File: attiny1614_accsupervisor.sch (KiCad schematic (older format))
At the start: 34 parts, among them J1 VXO7803-500-M-TR, J2 MSTBA_2,5_3-G, J3 Conn_01x02, J4 Conn_02x20_Odd_Even, J5 AVR-UPDI-6, K1 JSM1-12V-5, Q1 BC817, Q2 BC817, Q3 BC817, Q4 BSS84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

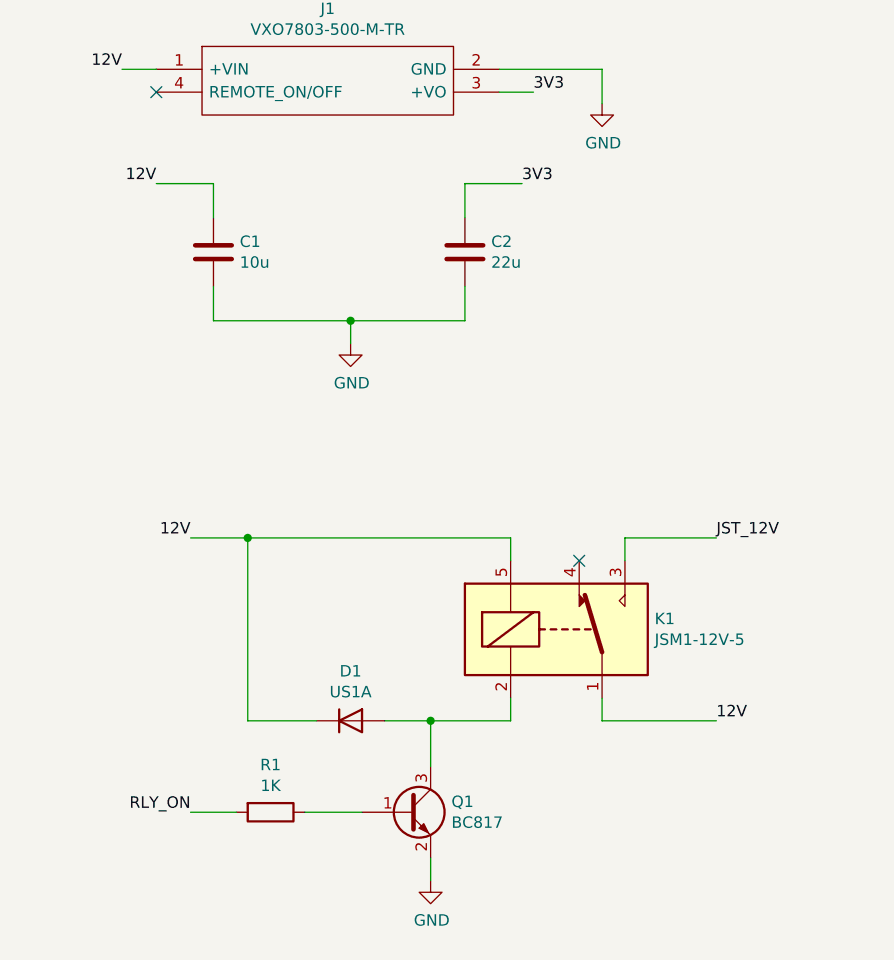
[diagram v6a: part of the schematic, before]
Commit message: BOM consolidation, 10/22uF to 4.7uFs
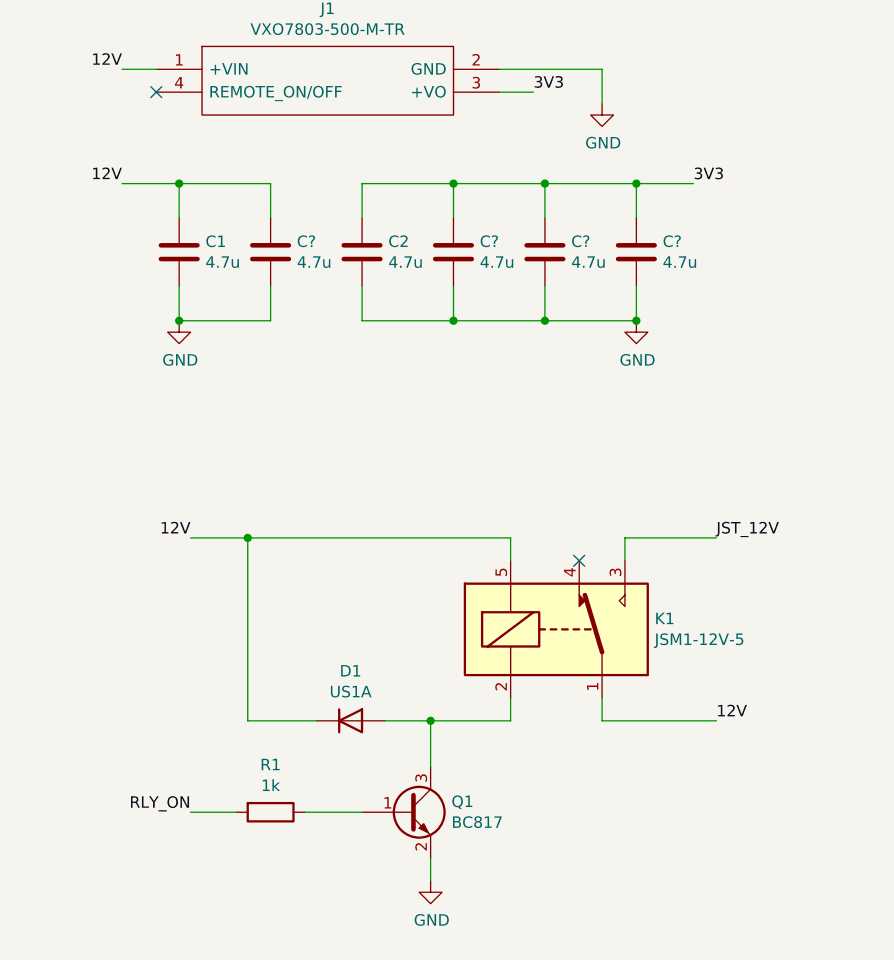
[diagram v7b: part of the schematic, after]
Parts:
- added C? (x4): 4.7u, Capacitor_SMD:C_0805_2012Metric_Pad1.15x1.40mm_HandSolder, symbol Device:C
- C1: value 10u -> 4.7u; footprint Capacitor_SMD:C_1206_3216Metric_Pad1.42x1.75mm_HandSolder -> Capacitor_SMD:C_0805_2012Metric_Pad1.15x1.40mm_HandSolder
- C2: value 22u -> 4.7u; footprint Capacitor_SMD:C_1206_3216Metric_Pad1.42x1.75mm_HandSolder -> Capacitor_SMD:C_0805_2012Metric_Pad1.15x1.40mm_HandSolder
- R1: value 1K -> 1k
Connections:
- net 12V: now also C?.1
- net 3V3: now also C?.1, C?.1, C?.1
- net GND: now also C?.2, C?.2, C?.2, C?.2
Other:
- moved on the sheet: C1, C2
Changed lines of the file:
@@
 P 1750 6150
 F 0 "R1" V 1543 6150 50  0000 C CNN
-F 1 "1K" V 1634 6150 50  0000 C CNN
+F 1 "1k" V 1634 6150 50  0000 C CNN
 F 2 "Resistor_SMD:R_1206_3216Metric_Pad1.42x1.75mm_HandSolder" V 1680 6150 50  0001 C CNN
 F 3 "~" H 1750 6150 50  0001 C CNN
@@
 L Device:C C1
 U 1 1 5F4FA9CB
-P 1500 3700
-F 0 "C1" H 1615 3746 50  0000 L CNN
-F 1 "10u" H 1615 3655 50  0000 L CNN
-F 2 "Capacitor_SMD:C_1206_3216Metric_Pad1.42x1.75mm_HandSolder" H 1538 3550 50  0001 C CNN
-F 3 "~" H 1500 3700 50  0001 C CNN
-	1    1500 3700
+P 1350 3700
+F 0 "C1" H 1465 3746 50  0000 L CNN
+F 1 "4.7u" H 1465 3655 50  0000 L CNN
+F 2 "Capacitor_SMD:C_0805_2012Metric_Pad1.15x1.40mm_HandSolder" H 1388 3550 50  0001 C CNN
+F 3 "~" H 1350 3700 50  0001 C CNN
+	1    1350 3700
 	1    0    0    -1
 $EndComp
@@
 L Device:C C2
 U 1 1 5F4FB924
-P 2600 3700
-F 0 "C2" H 2715 3746 50  0000 L CNN
-F 1 "22u" H 2715 3655 50  0000 L CNN
-F 2 "Capacitor_SMD:C_1206_3216Metric_Pad1.42x1.75mm_HandSolder" H 2638 3550 50  0001 C CNN
-F 3 "~" H 2600 3700 50  0001 C CNN
-	1    2600 3700
-	1    0    0    -1
-$EndComp
-Wire Wire Line
-	1500 3550 1500 3400
-Wire Wire Line
-	1500 3400 1250 3400
-Wire Wire Line
-	1500 3850 1500 4000
-Wire Wire Line
-	1500 4000 2100 4000
-Wire Wire Line
-	2600 4000 2600 3850
-Wire Wire Line
-	2600 3550 2600 3400
-Text Label 1250 3400 2    50   ~ 0
+P 2150 3700
+F 0 "C2" H 2265 3746 50  0000 L CNN
+F 1 "4.7u" H 2265 3655 50  0000 L CNN
+F 2 "Capacitor_SMD:C_0805_2012Metric_Pad1.15x1.40mm_HandSolder" H 2188 3550 50  0001 C CNN
+F 3 "~" H 2150 3700 50  0001 C CNN
+	1    2150 3700
+	1    0    0    -1
+$EndComp
+Wire Wire Line
+	1350 3550 1350 3400
+Wire Wire Line
+	1350 3400 1100 3400
+Wire Wire Line
+	1350 3850 1350 4000
+Wire Wire Line
+	1350 4000 1750 4000
+Wire Wire Line
+	2150 4000 2150 3850
+Wire Wire Line
+	2150 3550 2150 3400
+Text Label 1100 3400 2    50   ~ 0
 12V
-Wire Wire Line
-	2600 3400 2850 3400
-Text Label 2850 3400 0    50   ~ 0
+Text Label 3600 3400 0    50   ~ 0
 3V3
-Wire Wire Line
-	2100 4000 2100 4100
-Connection ~ 2100 4000
-Wire Wire Line
-	2100 4000 2600 4000
 $Comp
 L power:GND #PWR03
 U 1 1 5F5031AF
-P 2100 4100
-F 0 "#PWR03" H 2100 3850 50  0001 C CNN
-F 1 "GND" H 2105 3927 50  0000 C CNN
-F 2 "" H 2100 4100 50  0001 C CNN
-F 3 "" H 2100 4100 50  0001 C CNN
-	1    2100 4100
+P 1350 4000
+F 0 "#PWR03" H 1350 3750 50  0001 C CNN
+F 1 "GND" H 1355 3827 50  0000 C CNN
+F 2 "" H 1350 4000 50  0001 C CNN
+F 3 "" H 1350 4000 50  0001 C CNN
+	1    1350 4000
 	1    0    0    -1
 $EndComp
@@
 NoConn ~ 6250 1750
 NoConn ~ 6250 1850
+$Comp
+L Device:C C?
+U 1 1 5F5B52F6
+P 1750 3700
+F 0 "C?" H 1865 3746 50  0000 L CNN
+F 1 "4.7u" H 1865 3655 50  0000 L CNN
+F 2 "Capacitor_SMD:C_0805_2012Metric_Pad1.15x1.40mm_HandSolder" H 1788 3550 50  0001 C CNN
+F 3 "~" H 1750 3700 50  0001 C CNN
+	1    1750 3700
+	1    0    0    -1
+$EndComp
+Wire Wire Line
+	1750 3850 1750 4000
+Wire Wire Line
+	1750 3550 1750 3400
+Wire Wire Line
+	1750 3400 1350 3400
+Connection ~ 1350 3400
+$Comp
+L power:GND #PWR?
+U 1 1 5F5C8092
+P 3350 4000
+F 0 "#PWR?" H 3350 3750 50  0001 C CNN
+F 1 "GND" H 3355 3827 50  0000 C CNN
+F 2 "" H 3350 4000 50  0001 C CNN
+F 3 "" H 3350 4000 50  0001 C CNN
+	1    3350 4000
+	1    0    0    -1
+$EndComp
+$Comp
+L Device:C C?
+U 1 1 5F5D96DE
+P 2550 3700
+F 0 "C?" H 2665 3746 50  0000 L CNN
+F 1 "4.7u" H 2665 3655 50  0000 L CNN
+F 2 "Capacitor_SMD:C_0805_2012Metric_Pad1.15x1.40mm_HandSolder" H 2588 3550 50  0001 C CNN
+F 3 "~" H 2550 3700 50  0001 C CNN
+	1    2550 3700
+	1    0    0    -1
+$EndComp
+$Comp
+L Device:C C?
+U 1 1 5F5D99D3
+P 2950 3700
+F 0 "C?" H 3065 3746 50  0000 L CNN
+F 1 "4.7u" H 3065 3655 50  0000 L CNN
+F 2 "Capacitor_SMD:C_0805_2012Metric_Pad1.15x1.40mm_HandSolder" H 2988 3550 50  0001 C CNN
+F 3 "~" H 2950 3700 50  0001 C CNN
+	1    2950 3700
+	1    0    0    -1
+$EndComp
+$Comp
+L Device:C C?
+U 1 1 5F5D9D40
+P 3350 3700
+F 0 "C?" H 3465 3746 50  0000 L CNN
+F 1 "4.7u" H 3465 3655 50  0000 L CNN
+F 2 "Capacitor_SMD:C_0805_2012Metric_Pad1.15x1.40mm_HandSolder" H 3388 3550 50  0001 C CNN
+F 3 "~" H 3350 3700 50  0001 C CNN
+	1    3350 3700
+	1    0    0    -1
+$EndComp
+Wire Wire Line
+	2150 3400 2550 3400
+Wire Wire Line
+	2550 3550 2550 3400
+Connection ~ 2550 3400
+Wire Wire Line
+	2550 3400 2950 3400
+Wire Wire Line
+	2950 3550 2950 3400
+Connection ~ 2950 3400
+Wire Wire Line
+	2950 3400 3350 3400
+Wire Wire Line
+	3350 3550 3350 3400
+Connection ~ 3350 3400
+Wire Wire Line
+	3350 3400 3600 3400
+Wire Wire Line
+	3350 3850 3350 4000
+Wire Wire Line
+	3350 4000 2950 4000
+Wire Wire Line
+	2550 3850 2550 4000
+Connection ~ 2550 4000
+Wire Wire Line
+	2550 4000 2150 4000
+Wire Wire Line
+	2950 3850 2950 4000
+Connection ~ 2950 4000
+Wire Wire Line
+	2950 4000 2550 4000
+Connection ~ 1350 4000
+Connection ~ 3350 4000
 $EndSCHEMATC

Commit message: Gerber generated, r01
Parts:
- C1, C2: Manufacturer_Name (none) -> Walsin; Manufacturer_Part_Number (none) -> 0805X475M250CT
- C3, F2, H1, J2, J3, J4, J5, R13, R15, R6, R7, U1: Manufacturer_Name (none) -> -; Manufacturer_Part_Number (none) -> -
- C4, C5, C6, C7: renamed from C?; Manufacturer_Name (none) -> Walsin; Manufacturer_Part_Number (none) -> 0805X475M250CT
- D1: Manufacturer_Name (none) -> Diodes Inc.; Manufacturer_Part_Number (none) -> US1A-13-F
- F1: Manufacturer_Name (none) -> (Generic); Manufacturer_Part_Number (none) -> (10A)
- K1: Manufacturer_Name (none) -> Panasonic; Manufacturer_Part_Number (none) -> JSM1-12V-5
- Q1, Q2, Q3: Manufacturer_Name (none) -> Nexperia; Manufacturer_Part_Number (none) -> BC817-25,215
- Q4, Q5: Manufacturer_Name (none) -> Diodes Inc.; Manufacturer_Part_Number (none) -> BSS84-7-F
- R1, R2, R3: Manufacturer_Name (none) -> (Generic); Manufacturer_Part_Number (none) -> (1k)
- R10, R11: Manufacturer_Name (none) -> (Generic); Manufacturer_Part_Number (none) -> (2.2k)
- R12, R14: Manufacturer_Name (none) -> (Generic); Manufacturer_Part_Number (none) -> (0)
- R4, R5, R8, R9: Manufacturer_Name (none) -> (Generic); Manufacturer_Part_Number (none) -> (10k)
